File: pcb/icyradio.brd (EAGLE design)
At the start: 150 x 100 mm, 362 parts, among them J701 TRSJACK, J702 TRSJACK, J703 TRSJACK, Q801 AO3400, Q802 AO3400, U1001 MIC23155, U1002 MIC23159, U1003 MIC2019, U1004 ADP150UJZ-1.8, U1005 ADP150UJZ-3.3, U1006 MIC94305, U1007 MIC94305, U101 EFM32GG11B420F2048GL112, U201 ATSAMS70Q21B-C, U301 ICE40HX8K-CT256, U401 DSC1211DE3-C0017, U402 LTC2206, U403 RT820T2, U501 ADL5385, U502 AD9117, U503 ADL5601, U601 DSC1201DE3-50M00000, U602 ADF4351, U701 TSCS25A3X1NDGXZAX, U702 CP2615, U801 ER-TFT035-6, U901 DSC1201DE3-50M00000, U902 SI5351C, X101 32.768 kHz, X401 DNP, X901 DNP

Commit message: PCB needs machine gunning
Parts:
- added C528: 200pF, Capacitor:CAP0603
- added CON301: FPC-40P, Generic Connector:FPC-40P
- added D1002, D1003, D101, D201, D501, D702: LED0603, LED:0603
- added D301: RGBLED, LED:5050
- added R1015: 820 Ohms, Resistor:RES0603
- added R1016: 100K Ohms, Resistor:RES0603
- added R106, R204: 10K Ohms, Resistor:RES0603
- added R302, R303, R304: 330 Ohms, Resistor:RES0603
- added R516: 100 Ohms, Resistor:RES0603
- added R722: 3.57 Ohms, Resistor:RES0603
- added TP1, TP2, TP3: TESTPOINT-0.7MM, PADs:PAD0.7MM
- C516: value 200pF -> 100nF
- C520: value 620pF -> 200pF
- C524: value 200pF -> 620pF
- R1012: value 100K Ohms -> 510 Ohms
- R1013: value 820 Ohms -> 330 Ohms
- R103: value 4.7K Ohms -> 330 Ohms
- R105, R711: value 10K Ohms -> 4.7K Ohms
- R203: value 10K Ohms -> 330 Ohms
- R508: value 50 Ohms -> 510 Ohms
- R512: value 10K Ohms -> 50 Ohms
- R514, R707: value 100 Ohms -> 10K Ohms
- R704: value 24K Ohms -> 510 Ohms
- R705: value 47K Ohms -> 24K Ohms
- R706: value 10K Ohms -> 47K Ohms
- R708: value 2.21K Ohms -> 100 Ohms
- R709, R713: value 4.7K Ohms -> 2.21K Ohms
- R712: value 2.21K Ohms -> 10K Ohms
- R715: value 100 Ohms -> 4.7K Ohms
- R716: value 600 Ohms -> 100 Ohms
- R718, R721: value 3.57 Ohms -> 600 Ohms
- R719: value 600 Ohms -> 3.57 Ohms
- U801: device BuyDisplay:ZIF50 -> BuyDisplay:FPC-50P
- moved R1013 131.5 mm to (145.1, 70.6), turned to 180 degrees
- moved R1012 121.3 mm to (129.0, 94.6), turned to 180 degrees
- moved R1014 108.6 mm to (10.2, 70.0)
- moved U$2 68.3 mm to (70.9, 73.6)
- moved R203 41.3 mm to (101.2, 60.7), turned to 180 degrees
- moved R711 34.1 mm to (134.7, 19.9)
- moved R105 32.5 mm to (117.6, 34.6), turned to 0 degrees
- moved R715 30.0 mm to (145.3, 19.9), turned to 270 degrees
- moved R718 30.0 mm to (136.5, 16.6)
- moved R721 30.0 mm to (143.5, 16.6)
- moved R103 28.8 mm to (110.3, 60.7)
- moved U$1 26.6 mm to (41.8, 50.8)
- moved R712 26.2 mm to (100.8, 16.6), turned to 270 degrees
- moved R719 22.1 mm to (106.5, 16.6)
- moved R708 18.5 mm to (104.7, 19.9)
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- renumbered SJ1 to SJ201
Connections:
- net !DSP_SPI_SS renamed !DSP_SPI_CS
- removed net VPP_FAST: U301.D12
- new net DSP_LED: R203.2, U201.A12
- new net FPGA_BLED: R304.1, U301.B16
- new net FPGA_GLED: R303.1, U301.A15
- new net FPGA_RLED: R302.1, U301.A16
- new net N$105: CON301.5, U301.E3
- new net N$106: CON301.4, U301.E4
- new net N$107: CON301.3, U301.E5
- new net N$108: CON301.6, U301.E2
- new net N$109: CON301.9, U301.F1
- new net N$110: CON301.8, U301.F2
- new net N$111: CON301.7, U301.F3
- new net N$112: CON301.10, U301.G2
- new net N$113: CON301.12, U301.H2
- new net N$114: CON301.11, U301.G1
- new net N$115: CON301.13, U301.H1
- new net N$116: CON301.16, U301.J2
- new net N$117: CON301.15, U301.J1
- new net N$118: CON301.14, U301.H3
- new net N$119: CON301.18, U301.L1
- new net N$120: CON301.17, U301.K1
- new net N$121: CON301.23, U301.K3
- new net N$122: CON301.26, U301.L3
- new net N$123: CON301.24, U301.K4
- new net N$124: CON301.25, U301.L4
- new net N$125: CON301.27, U301.M1
- new net N$126: CON301.28, U301.M2
- new net N$127: CON301.29, U301.M3
- new net N$128: CON301.30, U301.M4
- new net N$129: CON301.31, U301.M5
- new net N$130: CON301.33, U301.M6
- new net N$131: CON301.32, U301.L5
- new net N$132: CON301.37, U301.L6
- new net N$133: CON301.34, U301.P4
- new net N$134: CON301.35, U301.P5
- new net N$135: CON301.36, U301.N6
- new net N$136: CON301.38, U301.N7
- new net N$137: C516.1, U502.34
- new net N$138: TP1.TP, U201.B11
- new net N$139: TP2.TP, U201.H11
- new net N$140: TP3.TP, U301.D12
- new net N$141: D301.2, R302.2
- new net N$142: D301.1, R303.2
- new net N$143: D301.3, R304.2
- new net N$144: D101.2, R103.1
- new net N$145: D201.2, R203.1
- new net N$146: D501.2, R508.1
- new net N$147: D702.2, R704.1
- new net N$148: D1003.2, R1013.1
- new net N$149: D1002.2, R1012.1
- new net SMC_LED: R103.2, U101.B1
- net !DSP_RESET: now also R204.1, U101.J8; no longer R203.1
- net !I2S_BRG_CFG: now also R707.1; no longer R706.1
- net !I2S_BRG_RST: now also R712.1; no longer R711.1
- net !SMC_RESET: now also R106.1; no longer R105.1
- net !TXPA_OC: now also R1016.1; no longer R1014.1
- net 3V3: now also CON301.1, CON301.20, CON301.21, CON301.40, R1013.2, R1016.2, R106.2, R204.2, R707.2, R712.2; no longer R1014.2, R103.2, R203.2, R706.2, R711.2
- net 5V0: now also R1012.2
- net 5V0_ANA_TXPA_CLEAN: now also R508.2
- net AUDIO_I2C_SCL: now also R105.1; no longer R104.1
- net AUDIO_I2C_SDA: now also R104.1; no longer R103.1
- net CODEC_HP_L: now also R722.1; no longer R721.1
- net CODEC_HP_R: now also R719.1; no longer R718.1
- net CODEC_LINE_L: now also R721.1; no longer R720.1
- net CODEC_LINE_R: now also R718.1; no longer R717.1
- net CODEC_MIC_L: now also R720.1; no longer R719.1
- net CODEC_MIC_R: now also R717.1; no longer R716.1
- net GND: now also C517.2, C518.1, C519.2, C520.1, C521.2, C522.1, C523.2, C524.1, C525.2, C526.1, C527.2, C528.1, CON301.19, CON301.2, CON301.22, CON301.39, D1002.1, D1003.1, D101.1, D201.1, D301.4, D301.5, D301.6, D501.1, D702.1, R1014.1, R1015.1, R509.1, R510.2, R511.1, R512.2, R706.1, R708.1, R711.1, R716.1; no longer C517.1, C518.2, C519.1, C520.2, C521.1, C522.2, C523.1, C524.2, C525.1, C526.2, C527.1, R1012.1, R1013.1, R508.1, R509.2, R510.1, R511.2, R705.1, R707.1, R709.1, R713.1
- net I2S_BRG_VBUS: now also R705.2
- net I2S_BRG_VBUS_DET: now also R705.1, R706.2; no longer R704.1, R705.2
- net N$38: now also R709.1, R710.2, R717.2; no longer R708.1, R709.2, R716.2
- net N$39: now also R713.1, R714.2, R720.2; no longer R712.1, R713.2, R719.2
- net N$42: now also R711.2, R718.2; no longer R710.2, R717.2
- net N$44: now also R715.2, R721.2; no longer R714.2, R720.2
- net N$50: now also R722.2; no longer R721.2
- net N$52: now also R708.2; no longer R707.2
- net N$53: now also R716.2; no longer R715.2
- net N$54: now also R719.2; no longer R718.2
- net N$55: now also R709.2, R713.2; no longer R708.2, R712.2
- net N$73: now also C518.2, R510.1; no longer C517.2, R509.1
- net N$74: now also C517.1, R509.2; no longer C516.1, R508.2
- net N$75: now also C522.2; no longer C521.2
- net N$76: now also C521.1; no longer C520.1
- net N$80: now also C520.2, R512.1; no longer C519.2, R511.1
- net N$81: now also C519.1, R511.2; no longer C518.1, R510.2
- net N$82: now also C524.2; no longer C523.2
- net N$83: now also C523.1; no longer C522.1
- net N$94: now also R1015.2; no longer R1013.2
- net TXDAC_AUXI: now also R513.2; no longer R512.2
- net TXDAC_AUXQ: now also R514.2; no longer R513.2
- net TXMIXER_IBBN: now also C525.1, R515.2; no longer C524.1, R514.2
- net TXMIXER_IBBP: now also C526.2, R513.1, R515.1; no longer C525.2, R512.1, R514.1
- net TXMIXER_QBBN: now also C527.1, R516.2; no longer C526.1, R515.2
- net TXMIXER_QBBP: now also C528.2, R514.1, R516.1; no longer C527.2, R513.1, R515.1
- net TXPA_BIAS_EN: now also R1014.2; no longer R1012.2
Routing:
- net N$136: track 0.00 -> 65.2 mm, vias 0 -> 2
- net N$135: track 0.00 -> 64.1 mm, vias 0 -> 2
- net N$131: track 0.00 -> 63.6 mm, vias 0 -> 2
- net N$132: track 0.00 -> 63.4 mm, vias 0 -> 2
- net N$133: track 0.00 -> 61.4 mm, vias 0 -> 2
- net N$128: track 0.00 -> 60.9 mm, vias 0 -> 2
- net N$123: track 0.00 -> 60.8 mm, vias 0 -> 2
- net N$106: track 0.00 -> 60.8 mm, vias 0 -> 2
- net N$130: track 0.00 -> 60.2 mm, vias 0 -> 2
- net N$122: track 0.00 -> 59.9 mm, vias 0 -> 2
- net N$134: track 0.00 -> 59.4 mm, vias 0 -> 2
- net N$129: track 0.00 -> 58.9 mm, vias 0 -> 2
- net N$107: track 0.00 -> 58.8 mm, vias 0 -> 2
- net N$108: track 0.00 -> 58.8 mm, vias 0 -> 2
- net N$118: track 0.00 -> 58.7 mm, vias 0 -> 2
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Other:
- board text added: "DSP Debug"
- board text added: "JLCJLCJLCJLC"
- board text added: "LINE IN"
- board text added: "MIC IN"
- board text added: "Mixer OUT"
- board text added: "OUT"
- board text added: "Power + DSP USB HS"
- board text added: "RF IN +10dBm Max"
- board text added: "RF OUT"
- board text added: "SMC Debug"
- board text added: "USB I²S Bridge"

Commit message: I think it dun
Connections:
- net N$1 renamed SMC_VCORE
- net N$100 renamed TXPLL_REF_DCC
- net N$105 renamed EXP_IO2
- net N$106 renamed EXP_IO1
- net N$107 renamed EXP_IO0
- net N$108 renamed EXP_IO3
- net N$109 renamed EXP_IO6
- net N$11 renamed CLK_MNGR_CLK1
- net N$110 renamed EXP_IO5
- net N$111 renamed EXP_IO4
- net N$112 renamed EXP_IO7
- net N$113 renamed EXP_IO9
- net N$114 renamed EXP_IO8
- net N$115 renamed EXP_IO10
- net N$116 renamed EXP_IO13
- net N$117 renamed EXP_IO12
- net N$118 renamed EXP_IO11
- net N$119 renamed EXP_IO15
- net N$12 renamed CLK_MNGR_CLK2
- net N$120 renamed EXP_IO14
- net N$121 renamed EXP_IO16
- net N$122 renamed EXP_IO19
- net N$123 renamed EXP_IO17
- net N$124 renamed EXP_IO18
- net N$125 renamed EXP_IO20
- net N$126 renamed EXP_IO21
- net N$127 renamed EXP_IO22
- net N$128 renamed EXP_IO23
- net N$129 renamed EXP_IO24
- net N$13 renamed CLK_MNGR_CLK3
- net N$130 renamed EXP_IO26
- net N$131 renamed EXP_IO25
- net N$132 renamed EXP_IO30
- net N$133 renamed EXP_IO27
- net N$134 renamed EXP_IO28
- net N$135 renamed EXP_IO29
- net N$136 renamed EXP_IO31
- net N$138 renamed DSP_JTAGSEL
- net N$139 renamed DSP_TST
- net N$14 renamed CLK_MNGR_CLK5
- net N$140 renamed FPGA_VPP_FAST
- net N$19 renamed CLK_MNGR_CLK6
- net N$2 renamed TXMIXER_OUT
- net N$24 renamed TFT_BL_K2
- net N$25 renamed TFT_BL_K1
- net N$28 renamed RXADC_SENSE
- net N$31 renamed CODEC_CAP-
- net N$32 renamed CPDEC_CAP+
- net N$33 renamed CODEC_V-
- net N$34 renamed CODEC_VREF
- net N$35 renamed CODEC_AFILT2
- net N$36 renamed CODEC_AFILT1
- net N$40 renamed 3V3_SOFTSTART
- net N$41 renamed 1V2_SOFTSTART
- net N$57 renamed TXPA_IN
- net N$59 renamed RXADC_ENC+
- net N$60 renamed CLK_MNGR_REF
- net N$61 renamed CLK_MNGR_XTALB
- net N$62 renamed CLK_MNGR_XTALA
- net N$66 renamed 3V6_ANA_SOFTSTART
- net N$7 renamed CLK_MNGR_CLK0
- net N$78 renamed TXPLL_CP_VOUT
- net N$79 renamed TXPLL_VTUNE
- net N$85 renamed TXPLL_TEMP
- net N$86 renamed TXPLL_VCOM
- net N$87 renamed TXPLL_VREF
- net N$89 renamed TXPLL_REF_ACC
- net N$90 renamed TXPA_OUT
- net N$91 renamed DSP_VDDPLLUSB
- net N$99 renamed TXPLL_FASTLOCK_SW
- net RXTUNER_PLL_VDD renamed RXTUNER_VDD_PLL
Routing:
- net 1V2: track 100.2 -> 98.1 mm
- net 3V3: track 501.5 -> 499.4 mm
- net GND: vias 169 -> 1727

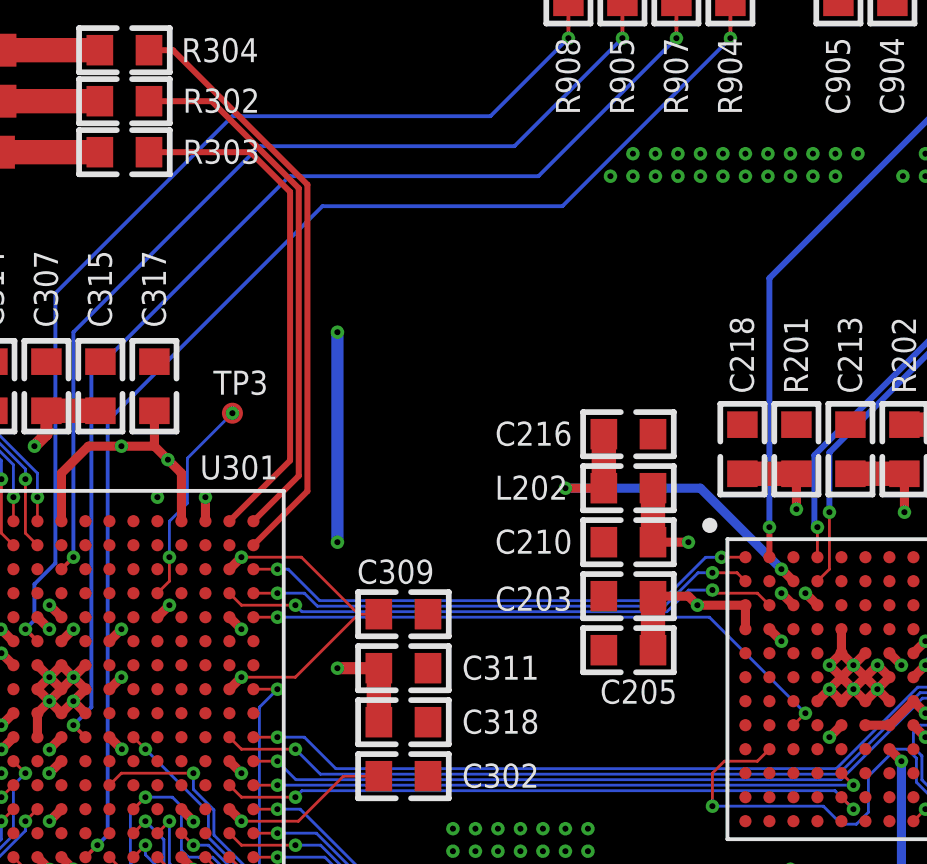
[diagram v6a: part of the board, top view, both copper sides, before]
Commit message: Added FPGA SPI memory
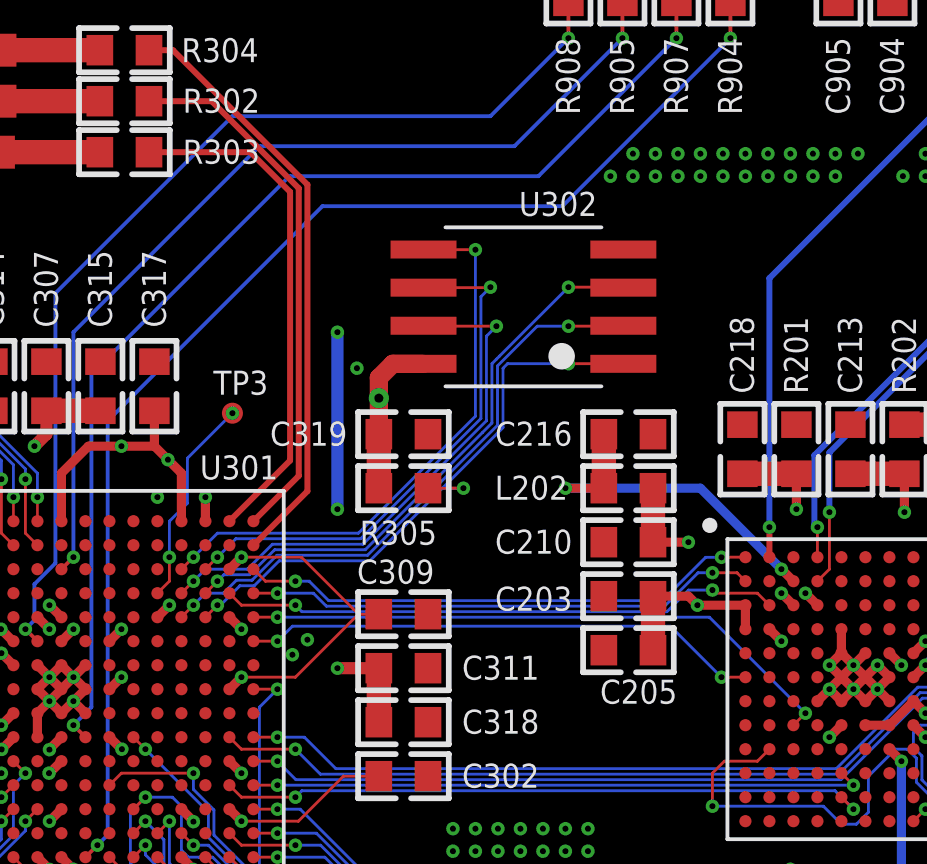
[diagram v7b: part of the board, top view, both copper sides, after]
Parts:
- added C319: 100nF, Capacitor:CAP0603
- added R305: 100K Ohms, Resistor:RES0603
- added U302: SST26VF064B, Microchip:WSOIC8
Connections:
- net FPGA_DDC_CLK renamed FPGA_CLK1
- net FPGA_GP_CLK1 renamed FPGA_CLK2
- net FPGA_GP_CLK2 renamed FPGA_CLK3
- net FPGA_GP_CLK3 renamed FPGA_CLK4
- new net !FPGA_DSP_IRQ: U201.F1, U301.F16
- new net !FPGA_MEM_CS: R305.1, U301.E14, U302.1
- new net FPGA_MEM_IO0: U301.C13, U302.5
- new net FPGA_MEM_IO1: U301.E13, U302.2
- new net FPGA_MEM_IO2: U301.D14, U302.3
- new net FPGA_MEM_IO3: U301.D13, U302.7
- new net FPGA_MEM_SCK: U301.C14, U302.6
- net 3V3: now also C319.1, R305.2, U302.8
- net GND: now also C319.2, U302.4
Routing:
- net !FPGA_MEM_CS: track 0.00 -> 20.5 mm, vias 0 -> 3
- net FPGA_MEM_IO1: track 0.00 -> 19.9 mm, vias 0 -> 2
- net FPGA_MEM_IO2: track 0.00 -> 19.3 mm, vias 0 -> 2
- net FPGA_MEM_IO0: track 0.00 -> 19.2 mm, vias 0 -> 2
- net FPGA_MEM_IO3: track 0.00 -> 18.3 mm, vias 0 -> 2
- net FPGA_MEM_SCK: track 0.00 -> 18.0 mm, vias 0 -> 2
- net !FPGA_DSP_IRQ: track 0.00 -> 17.3 mm, vias 0 -> 2
- net 3V3: track 499.4 -> 504.8 mm, vias 111 -> 112
- net GND: vias 1727 -> 1730

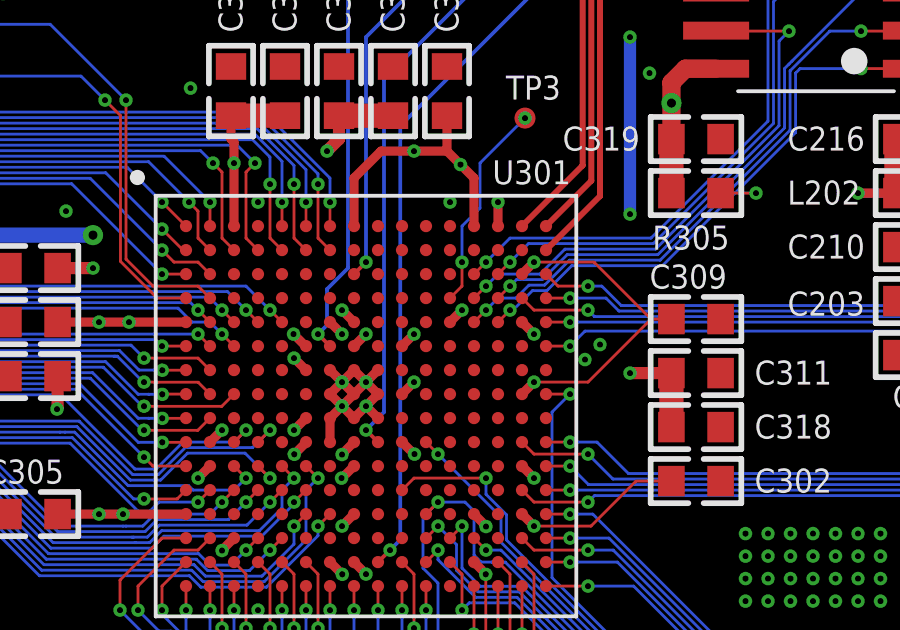
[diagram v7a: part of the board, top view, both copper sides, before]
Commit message: Fixed FPGA VCC_2V5 connected to 1V2
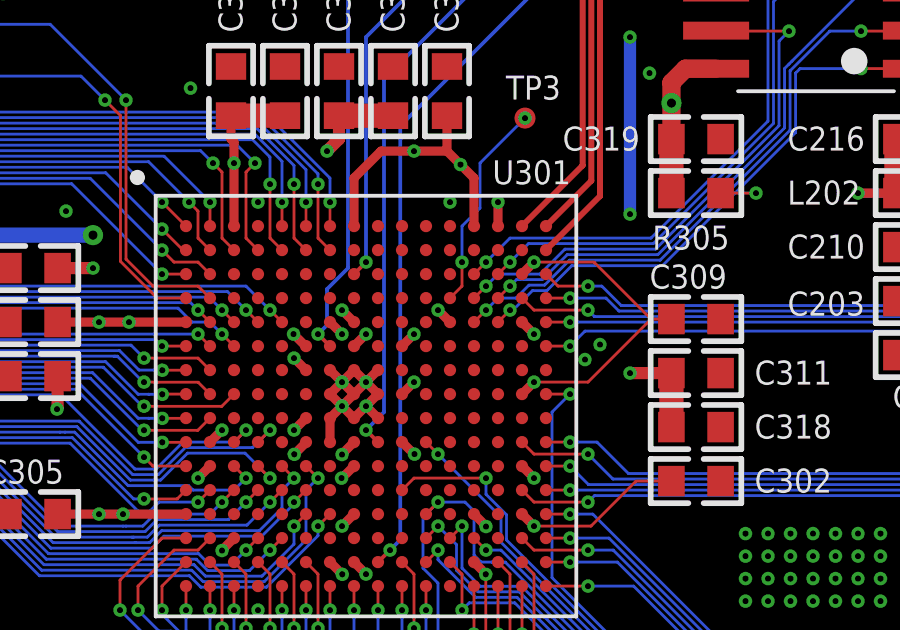
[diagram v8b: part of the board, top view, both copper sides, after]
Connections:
- net 1V2: no longer U301.E12
- net 3V3: now also U301.E12
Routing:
- net 1V2: track 98.1 -> 95.3 mm, vias 45 -> 44
- net 3V3: track 504.8 -> 505.3 mm, vias 112 -> 113
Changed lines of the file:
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@@
 <via x="76.28085" y="60.1" extent="1-16" drill="0.3"/>
 <wire x1="76.28085" y1="58.9" x2="76.28085" y2="57.1" width="0.8128" layer="1"/>
+<contactref element="U301" pad="E12"/>
+<wire x1="68.9" y1="52.8" x2="68.5" y2="53.2" width="0.3048" layer="1"/>
+<via x="68.5" y="53.2" extent="1-16" drill="0.2"/>
 </signal>
 <signal name="SMC_VCORE">
@@
 <wire x1="126.7348" y1="69.5" x2="124.3494" y2="69.5" width="1.27" layer="1"/>
 <wire x1="124.51915" y1="69.33025" x2="124.3494" y2="69.5" width="0.8128" layer="1"/>
-<wire x1="68.9" y1="52.8" x2="69.3" y2="53.2" width="0.3048" layer="1"/>
-<via x="69.3" y="53.2" extent="1-16" drill="0.2"/>
 <wire x1="67.3" y1="52" x2="67.7" y2="52.4" width="0.3048" layer="1"/>
 <via x="67.7" y="52.4" extent="1-16" drill="0.2"/>
@@
 <wire x1="67.1" y1="40.11915" x2="65.3" y2="40.11915" width="0.8128" layer="1"/>
 <contactref element="U301" pad="E8"/>
-<contactref element="U301" pad="E12"/>
 <contactref element="U301" pad="F6"/>
 <contactref element="U301" pad="F10"/>
@@
 <wire x1="57" y1="54.6" x2="55.4" y2="54.6" width="0.4064" layer="15"/>
 <wire x1="55.4" y1="54.6" x2="54.2" y2="55.8" width="0.4064" layer="15"/>
-<wire x1="69.3" y1="53.2" x2="65.7" y2="56.8" width="0.4064" layer="15"/>
+<wire x1="67.7" y1="54.4" x2="65.7" y2="56.4" width="0.4064" layer="15"/>
 <wire x1="65.7" y1="57.6" x2="64.8" y2="58.5" width="0.4064" layer="15"/>
-<wire x1="65.7" y1="56.8" x2="65.7" y2="57.6" width="0.4064" layer="15"/>
-<wire x1="65.3" y1="53.2" x2="65.3" y2="56.4" width="0.4064" layer="15"/>
-<wire x1="65.3" y1="56.4" x2="65.7" y2="56.8" width="0.4064" layer="15"/>
+<wire x1="65.7" y1="56.4" x2="65.7" y2="57.6" width="0.4064" layer="15"/>
+<wire x1="65.3" y1="53.2" x2="65.3" y2="56" width="0.4064" layer="15"/>
+<wire x1="65.3" y1="56" x2="65.7" y2="56.4" width="0.4064" layer="15"/>
 <wire x1="63.68516875" y1="52.4" x2="64.48516875" y2="53.2" width="0.4064" layer="15"/>
 <wire x1="64.48516875" y1="53.2" x2="65.3" y2="53.2" width="0.4064" layer="15"/>
-<wire x1="67.7" y1="52.4" x2="68.5" y2="52.4" width="0.4064" layer="15"/>
-<wire x1="68.5" y1="52.4" x2="69.3" y2="53.2" width="0.4064" layer="15"/>
+<wire x1="67.7" y1="52.4" x2="67.7" y2="54.4" width="0.4064" layer="15"/>
 <wire x1="67.71483125" y1="48.4" x2="68.91483125" y2="49.6" width="0.4064" layer="15"/>
 <wire x1="68.91483125" y1="49.6" x2="73.4" y2="49.6" width="0.4064" layer="15"/>
